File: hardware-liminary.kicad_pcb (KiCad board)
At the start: 2 copper layers, 149.2 x 73 mm, 55 parts, among them IC1 MCP6001T-I_OT, J3 UFL-Conn, J4 SWD, J5 Console, J6 Nema 7-Pin, K1 HL2-1CH-12S, Q1 CMBT2222A, Q2 PT204-6C, Q3 CMBT3904, SW1 SW_Push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

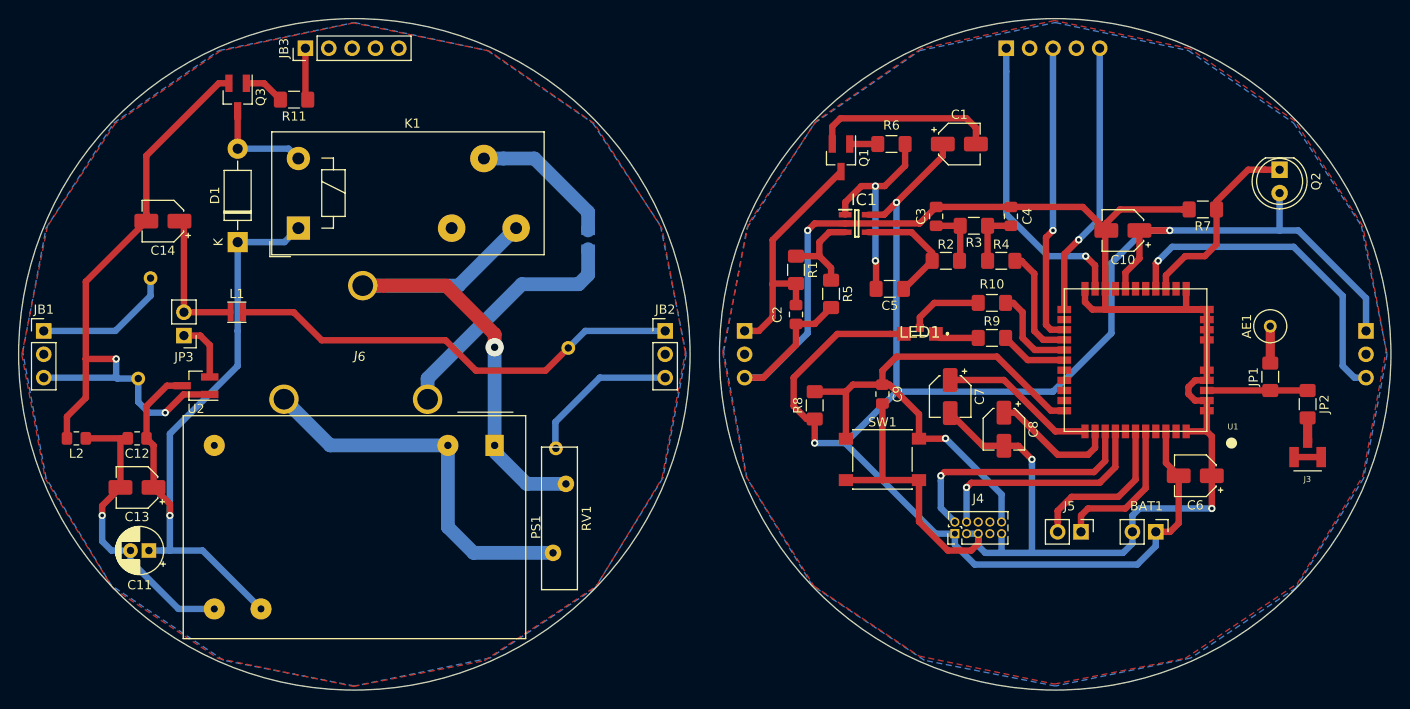
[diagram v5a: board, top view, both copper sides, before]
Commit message: Agregado modulo de medicion de energia a pcb
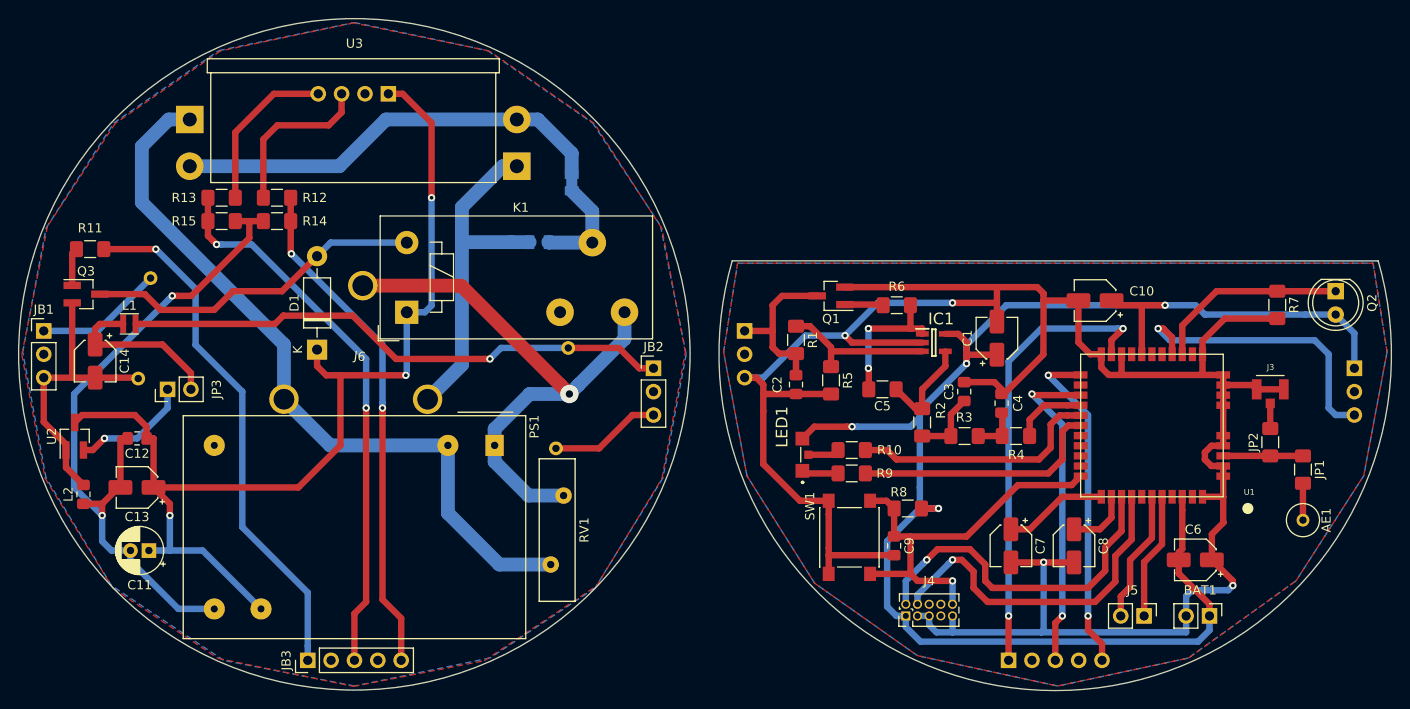
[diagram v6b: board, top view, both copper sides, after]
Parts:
- added JP5: Jumper_2_Open, Jumper:SolderJumper-2_P1.3mm_Open_Pad1.0x1.5mm, B.Cu at (131.8, 76.3)
- added R12: 10K, Resistor_SMD:R_1206_3216Metric_Pad1.42x1.75mm_HandSolder, F.Cu at (99.8, 78.0)
- added R13: 10K, Resistor_SMD:R_1206_3216Metric_Pad1.42x1.75mm_HandSolder, F.Cu at (93.8, 78.0)
- added R14: 20K, Resistor_SMD:R_1206_3216Metric_Pad1.42x1.75mm_HandSolder, F.Cu at (99.8, 80.5)
- added R15: 20K, Resistor_SMD:R_1206_3216Metric_Pad1.42x1.75mm_HandSolder, F.Cu at (93.8, 80.5)
- added U3: HLW8032_module, proyect_new:HLW8032_module_vertical, F.Cu at (108.1, 66.7)
- moved JB3 66.5 mm to (103.1, 128.3)
- moved JT3 66.5 mm to (179.3, 128.3)
- moved R11 27.5 mm to (79.5, 83.6)
- moved Q3 27.0 mm to (79.0, 88.5), turned to 0 degrees
- moved R3 22.9 mm to (174.5, 103.9)
- moved R10 22.1 mm to (162.3, 105.4)
- moved C1 21.5 mm to (178.1, 93.2), turned to 90 degrees
- moved AE1 21.4 mm to (211.3, 113.0), turned to 90 degrees
- moved R9 21.2 mm to (162.3, 108.0)
- moved C4 20.3 mm to (178.6, 100.3)
- moved C3 19.3 mm to (174.5, 99.1)
- moved R4 19.1 mm to (180.1, 103.9)
- moved LED1 18.3 mm to (157.2, 105.9), turned to 90 degrees
- moved R2 17.8 mm to (169.9, 102.4), turned to 90 degrees
- moved R6 17.5 mm to (167.2, 89.7)
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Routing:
- net /Bottom Board/Enery_Tx: track 0.00 -> 60.2 mm, vias 0 -> 2
- net /Bottom Board/Enery_Pulses: track 0.00 -> 55.3 mm, vias 0 -> 2
- net /Bottom Board/Relay: track 5.69 -> 57.2 mm, vias 0 -> 1
- net Net-(JP5-Pad2): track 0.00 -> 47.4 mm
- net GNDA: track 32.5 -> 76.3 mm, vias 1 -> 2
- net GNDREF: track 73.8 -> 31.9 mm, vias 2 -> 0
- net /Bottom Board/Neutro: track 40.4 -> 81.1 mm
- net /Bottom Board/+12v: track 76.4 -> 115.9 mm, vias 1 -> 3
- net /Top Board/3.3v: track 206.2 -> 172.3 mm, vias 3 -> 4
- net Net-(D1-Pad2): track 11.2 -> 37.1 mm
- net /Top Board/Led1: track 7.38 -> 27.3 mm
- net Net-(R12-Pad2): track 0.00 -> 18.1 mm
- net Net-(R13-Pad2): track 0.00 -> 17.9 mm
- net /Top Board/Relay: track 32.5 -> 49.7 mm, vias 1 -> 2
- net /Top Board/Led2: track 10.1 -> 27.3 mm
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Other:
- board size 149.2 x 73 mm -> 149.3 x 73.1 mm
- board text added: "Bottom Board"
- board text added: "Top Board"

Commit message: optimizacion de pistas
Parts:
- moved D1 17.0 mm to (109.2, 78.2), turned to 180 degrees
- moved R15 11.5 mm to (82.3, 81.3), turned to 0 degrees
- moved L1 9.55 mm to (92.5, 95.6), turned to 90 degrees
- moved R14 8.77 mm to (94.0, 87.1)
- moved R13 8.42 mm to (85.4, 78.7)
- moved R12 6.67 mm to (95.5, 83.1), turned to 90 degrees
- moved Q1 4.74 mm to (163.6, 91.8)
- moved R11 4.14 mm to (76.2, 86.1), turned to 270 degrees
- moved IC1 4.07 mm to (170.9, 97.8)
- moved R6 3.92 mm to (169.6, 92.7)
- moved C5 3.82 mm to (165.4, 102.6)
- moved R8 3.46 mm to (171.7, 112.5), turned to 0 degrees
- moved Q3 3.24 mm to (80.8, 91.2)
- moved C3 3.14 mm to (173.7, 102.1)
- moved R1 1.82 mm to (157.7, 94.5), turned to 180 degrees
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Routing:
- net GNDA: track 76.3 -> 119.3 mm
- net GNDD: track 259.6 -> 246.7 mm
- net Net-(D1-Pad2): track 37.1 -> 48.0 mm, vias 0 -> 1
- net /Bottom Board/3.3v: track 60.0 -> 50.5 mm
- net /Bottom Board/Enery_Tx: track 60.2 -> 66.8 mm
- net Net-(R13-Pad2): track 17.9 -> 23.7 mm
- net Net-(C14-Pad1): track 18.5 -> 12.8 mm
- net /Top Board/3.3v: track 172.3 -> 175.8 mm
- net Net-(R12-Pad2): track 18.1 -> 21.5 mm
- net /Top Board/Reset: track 44.9 -> 48.3 mm
- net Net-(IC1-Pad3): track 16.8 -> 13.6 mm
- net Net-(C5-Pad1): track 11.0 -> 7.97 mm
- net /Bottom Board/+12v: track 115.9 -> 113.4 mm
- net /Top Board/Led2: track 27.3 -> 29.7 mm
- net /Top Board/OpenC: track 18.1 -> 19.9 mm
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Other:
- net class Load: clearance 0.2 -> 0.8

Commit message: Mejoras en ruteo
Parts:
- moved R14 6.25 mm to (99.8, 84.8), turned to 90 degrees
- moved C10 3.75 mm to (185.4, 90.9)
- moved R11 2.88 mm to (79.0, 86.6), turned to 180 degrees
- moved R12 1.27 mm to (96.8, 83.1)
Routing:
- net GNDD: track 246.7 -> 233.3 mm
- net GNDA: track 119.3 -> 109.4 mm
- net /Bottom Board/Relay: track 58.5 -> 53.4 mm
- net /Top Board/3.3v: track 175.8 -> 180.1 mm
- net /Bottom Board/Enery_Pulses: track 54.8 -> 59.0 mm
- net /Bottom Board/Carga: track 36.1 -> 32.4 mm
- net Net-(D1-Pad2): track 48.0 -> 51.0 mm
- net /Bottom Board/+12v: track 113.4 -> 112.5 mm
- net /Bottom Board/Neutro: track 81.1 -> 81.7 mm
- net /Bottom Board/Enery_Tx: track 66.8 -> 66.2 mm
- net Net-(R12-Pad2): track 21.5 -> 21.0 mm
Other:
- net class Default: clearance 0.2 -> 0.25
- net class Load: clearance 0.8 -> 1
- rule trace_clearance: 0.2 -> 0.25
